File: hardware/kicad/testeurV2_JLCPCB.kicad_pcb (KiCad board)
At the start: 2 copper layers, 100 x 68 mm, 33 parts, among them P1 Power_pads, U1 TSR_2-2450, U2 MCP2551-I-SN, U3 NUCLEO32-L432KC, U4 PCA9554D, U5 MAX6818

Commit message: [Harware] Update to last version.
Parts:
- added REF**: MountingHole_2.2mm_M2, MountingHole:MountingHole_2.2mm_M2, F.Cu at (112.0, 127.0)
- added REF**: MountingHole_2.2mm_M2, MountingHole:MountingHole_2.2mm_M2, F.Cu at (206.0, 127.0)
- added REF**: MountingHole_2.2mm_M2, MountingHole:MountingHole_2.2mm_M2, F.Cu at (206.0, 65.0)
- added REF**: MountingHole_2.2mm_M2, MountingHole:MountingHole_2.2mm_M2, F.Cu at (112.0, 65.0)
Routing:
- net +5V: track 212.3 -> 215.3 mm
- added copper zone on B.Cu, net GND
- added copper zone on F.Cu, net GND
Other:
- board text added: "Servo Tester V2.1 - Fabien-B@ENAC - 2019"
- board text added: "Servo Tester V2.1 Fabien-B@ENAC 2019"
- board text added: "USB"

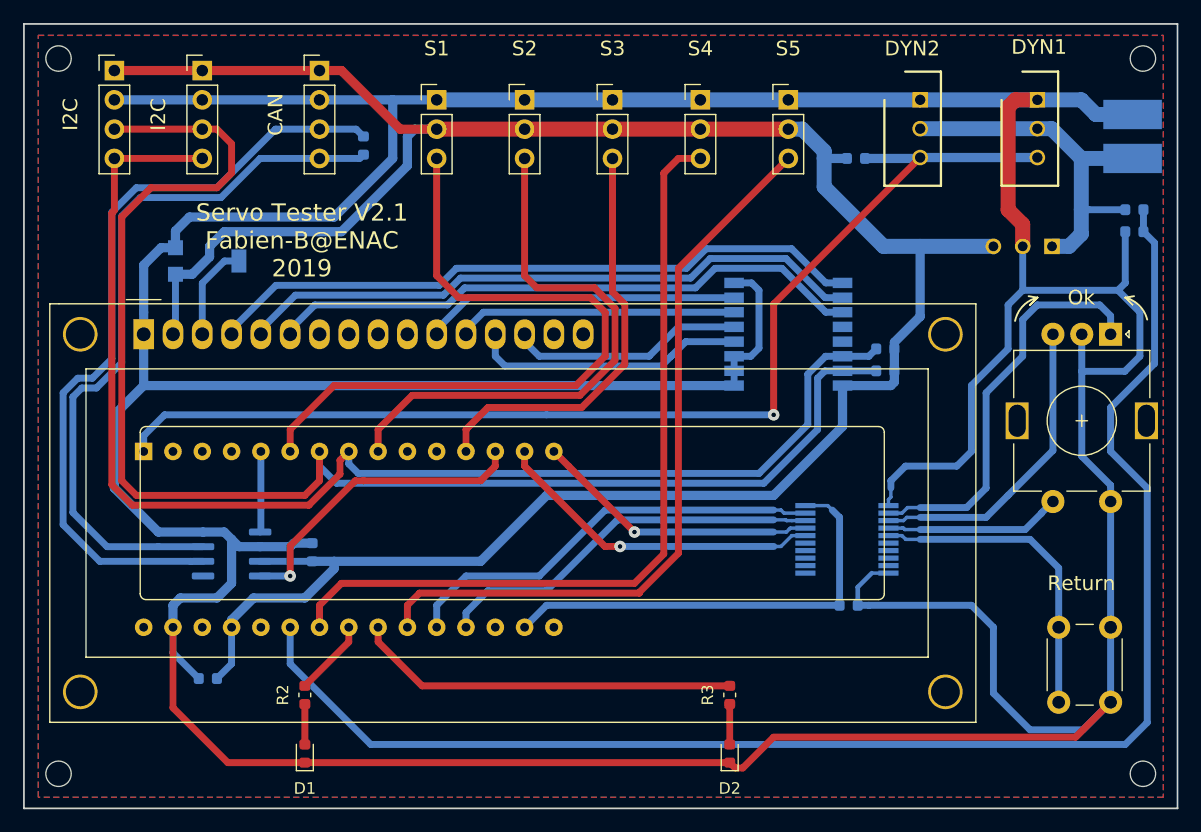
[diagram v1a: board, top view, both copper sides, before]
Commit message: Fix hardware and move to V2.3.
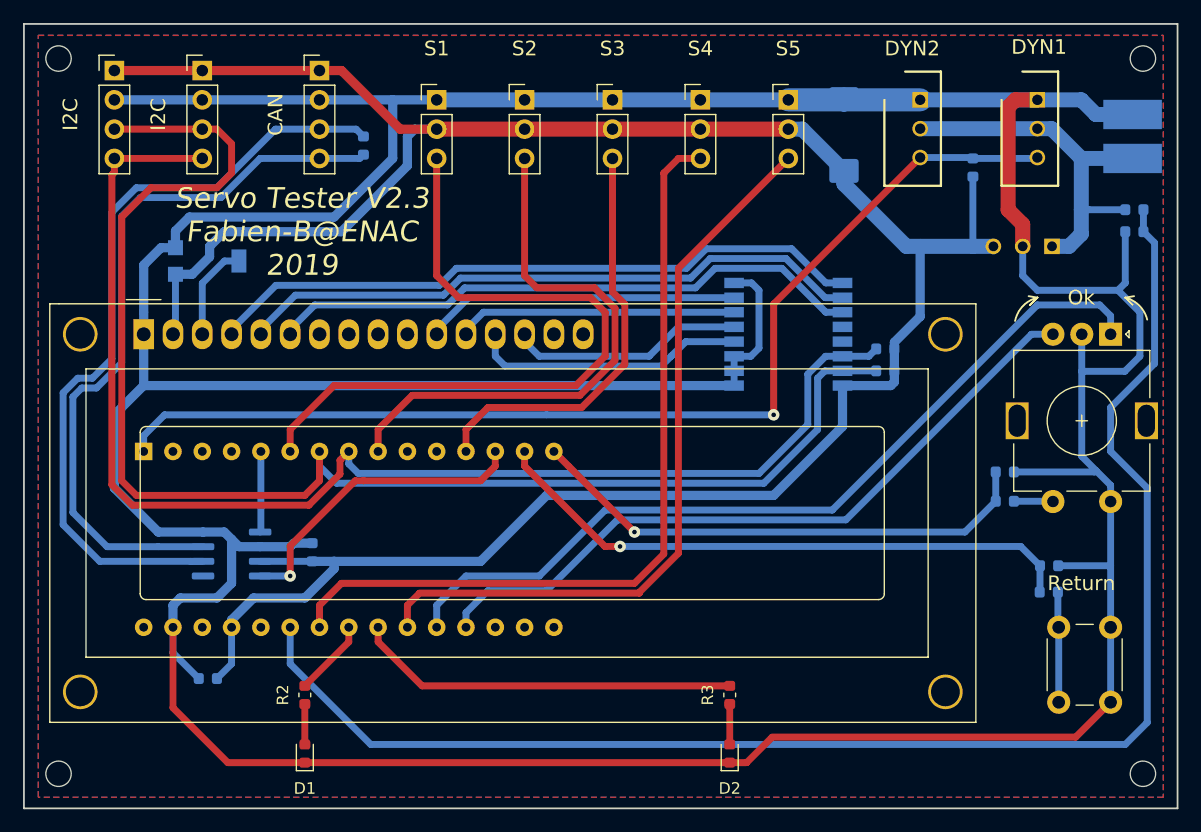
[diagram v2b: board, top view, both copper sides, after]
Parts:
- removed U5: MAX6818, Package_SO:SSOP-20_5.3x7.2mm_P0.65mm
- added C3: 330n, Capacitor_SMD:C_0603_1608Metric, B.Cu at (194.0, 100.8)
- added C5: 330n, Capacitor_SMD:C_0603_1608Metric, B.Cu at (197.9, 109.0)
- added R10: 10k, Resistor_SMD:R_0603_1608Metric, B.Cu at (197.8, 111.3)
- added R9: 10k, Resistor_SMD:R_0603_1608Metric, B.Cu at (194.0, 103.4)
- C2: value 100n -> CP; footprint Capacitor_SMD:C_0603_1608Metric -> Capacitor_Tantalum_SMD:CP_EIA-7343-31_Kemet-D
- moved C2 40.8 mm to (180.1, 71.6), turned to 90 degrees
- moved R6 10.2 mm to (191.3, 74.4), turned to 270 degrees
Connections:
- C2 pad 1: GND -> +5V
- C2 pad 2: +3V3 -> GND
- OK1 pad A: Net-(OK1-PadA) -> /ENC_A
- OK1 pad B: Net-(OK1-PadB) -> /ENC_B
- U3 pad 17: +3V3 -> (no net)
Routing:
- net GND: track 472.6 -> 421.7 mm
- net +3V3: track 39.1 -> 0.00 mm
- net /ENC_A: track 37.4 -> 73.1 mm
- net Net-(OK1-PadA): track 35.4 -> 0.00 mm
- net /ENC_B: track 34.0 -> 62.1 mm
- net Net-(OK1-PadB): track 26.9 -> 0.00 mm
- net /RET_BTN: track 28.9 -> 51.8 mm
- net /OK_BTN: track 24.8 -> 44.8 mm
- net Net-(R10-Pad2): track 27.6 -> 9.58 mm
- net Net-(OK1-PadS1): track 15.3 -> 3.39 mm
- net /DYNAMIXEL: track 99.3 -> 94.6 mm
- net +5V: track 215.3 -> 218.3 mm
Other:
- board text added: "+"
- board text added: "-"
- board text added: "Nucleo L432 remove SB9, SB16 and SB18"
- board text added: "Power with 3S battery"
- board text added: "Servo Tester V2.3 Fabien-B@ENAC 2019"
- board text removed: "Servo Tester V2.1 - Fabien-B@ENAC - 2019"
- board text removed: "Servo Tester V2.1 Fabien-B@ENAC 2019"

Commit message: Rename file + change some part names.
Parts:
- C1, C4: value 100n -> 100nF
- C2: value CP -> 100µF
- C3, C5: value 330n -> 330nF
- CAN1: value CAN -> J_01x04P2.54
- I2C1_a1: renamed from I2C1; value I2C_a -> J_01x04P2.54
- I2C1_b1: renamed from JI2C1; value I2C_b -> J_01x04P2.54
- R1: value 120 -> 120Ω
- R2, R3: value R -> 390Ω
- Ret1: value return -> Push_Switch
- S1: value S1 -> JServo
- S2: value S2 -> JServo
- S3: value S3 -> JServo
- S4: value S4 -> JServo
- S5: value S5 -> JServo
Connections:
- DS1 pad 10: (no net) -> Net-(DS1-Pad10)
- DS1 pad 15: (no net) -> Net-(DS1-Pad15)
- DS1 pad 16: (no net) -> Net-(DS1-Pad16)
- DS1 pad 7: (no net) -> Net-(DS1-Pad7)
- DS1 pad 8: (no net) -> Net-(DS1-Pad8)
- DS1 pad 9: (no net) -> Net-(DS1-Pad9)
- U2 pad 5: (no net) -> Net-(U2-Pad5)
- U3 pad 10: (no net) -> Net-(U3-Pad10)
- U3 pad 11: (no net) -> Net-(U3-Pad11)
- U3 pad 16: (no net) -> Net-(U3-Pad16)
- U3 pad 17: (no net) -> Net-(U3-Pad17)
- U3 pad 18: (no net) -> Net-(U3-Pad18)
- U3 pad 2: (no net) -> Net-(U3-Pad2)
- U3 pad 26: (no net) -> Net-(U3-Pad26)
- U3 pad 28: (no net) -> Net-(U3-Pad28)
- U3 pad 3: (no net) -> Net-(U3-Pad3)
- U3 pad 30: (no net) -> Net-(U3-Pad30)
- U3 pad 4: (no net) -> Net-(U3-Pad4)
- U4 pad 12: (no net) -> Net-(U4-Pad12)
- U4 pad 13: (no net) -> Net-(U4-Pad13)
